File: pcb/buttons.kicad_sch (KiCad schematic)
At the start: 21 parts, among them SW1 SW_DPDT_x2, SW2 SW_DPDT_x2, SW3 RotaryEncoder, SW4 SW_DPDT_x2, SW5 SW_DPDT_x2

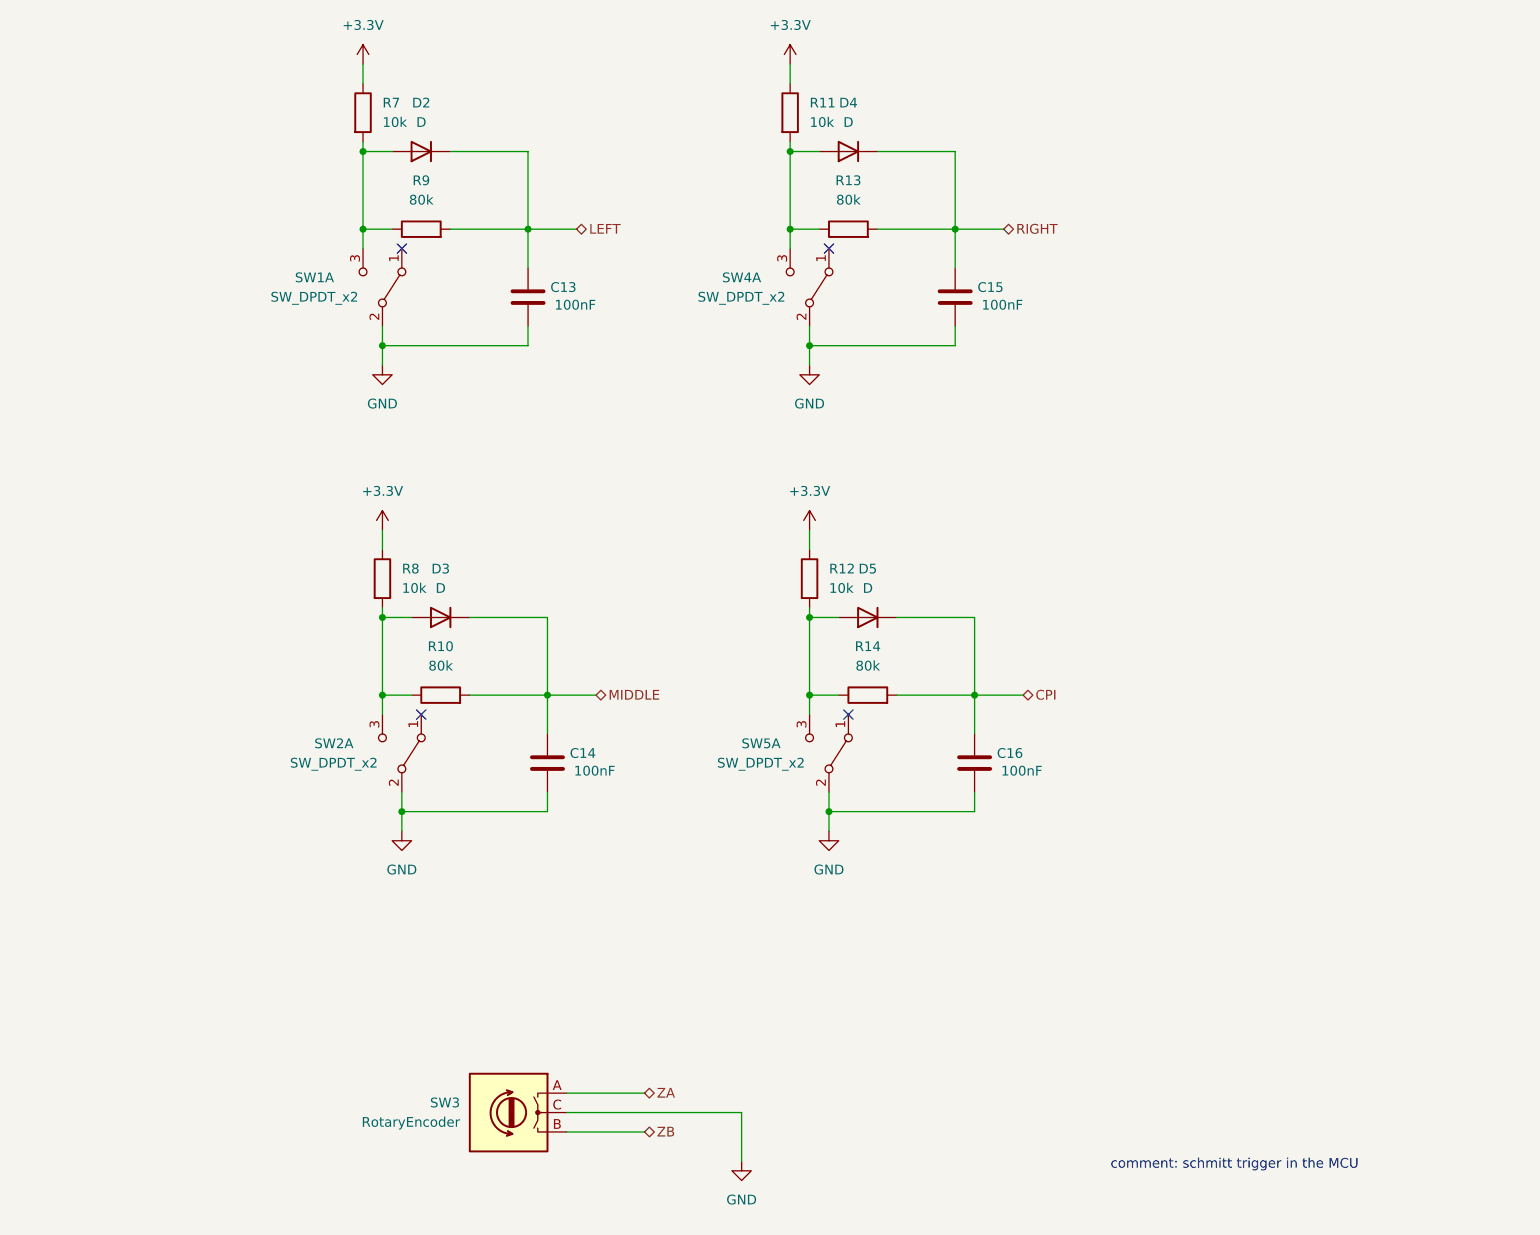
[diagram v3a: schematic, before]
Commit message: - added rotary encoder debouncing - added mouse switch and encoder footprints - changed some symbols - assigned footprints
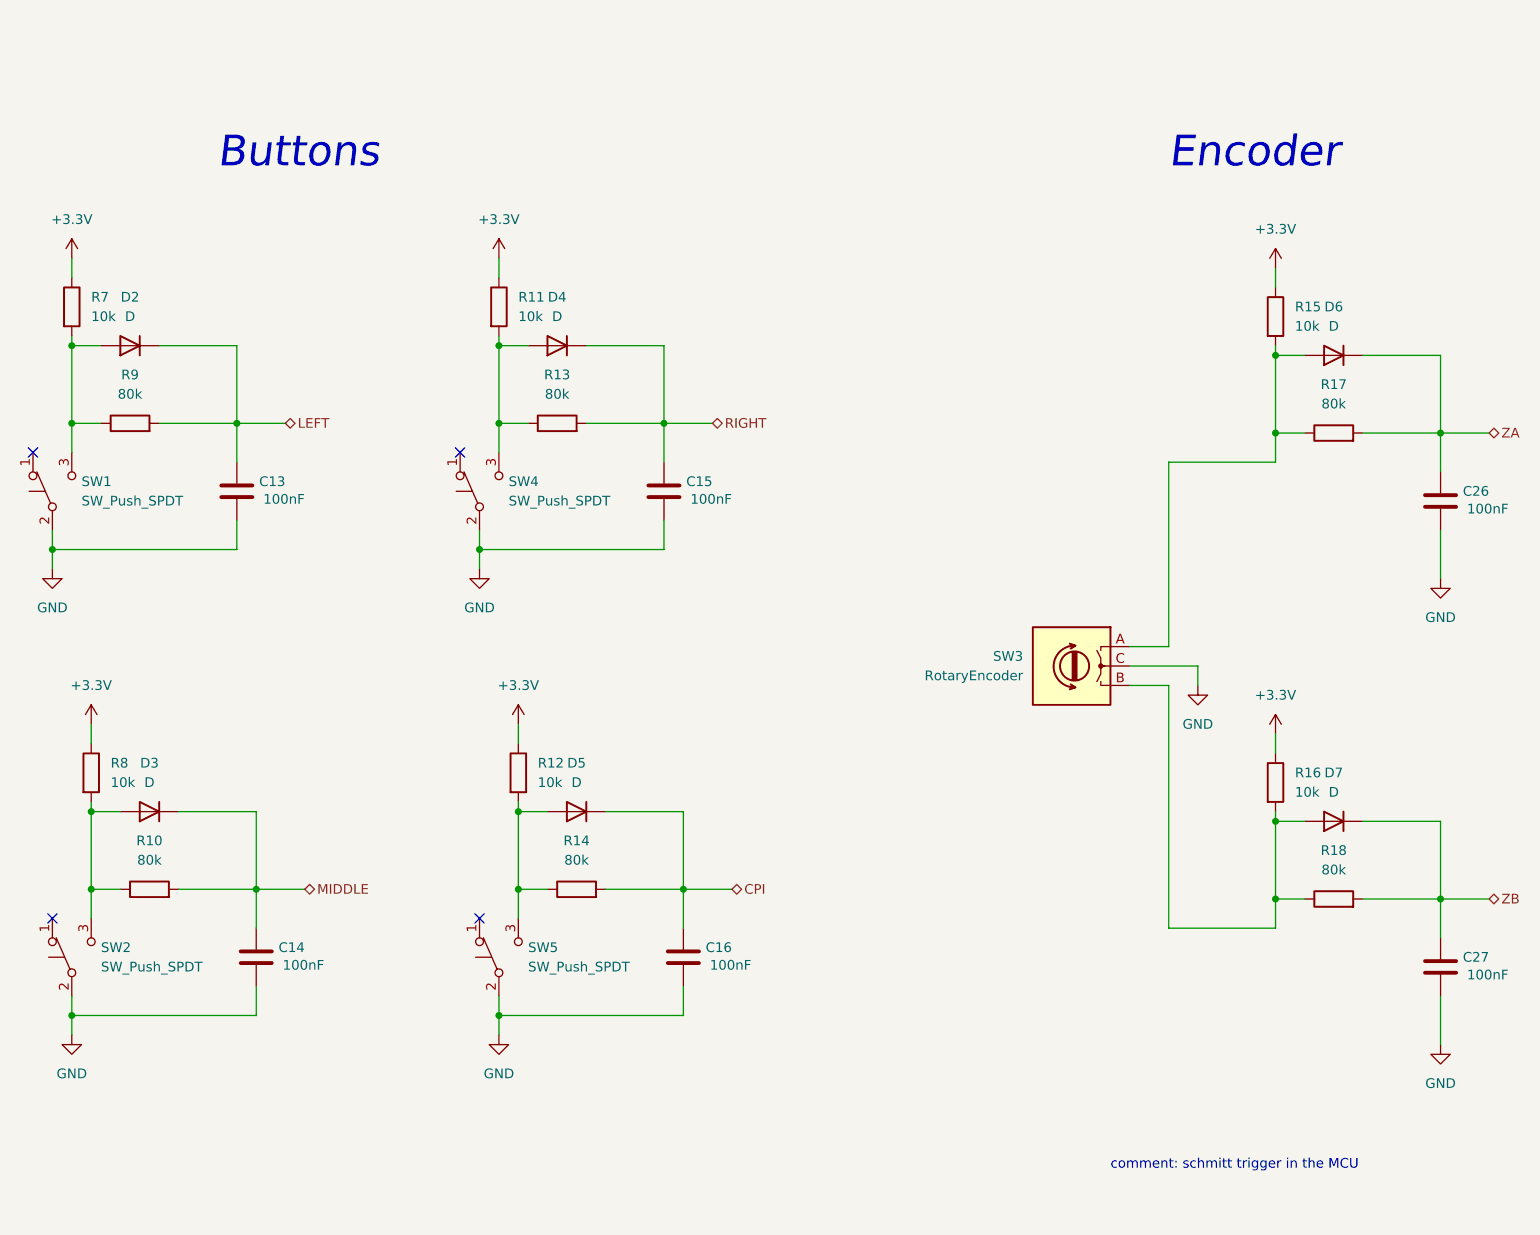
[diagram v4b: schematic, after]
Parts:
- removed SW1, SW2, SW4, SW5: SW_DPDT_x2, symbol Switch:SW_DPDT_x2
- added C26, C27: 100nF, Capacitor_SMD:C_0603_1608Metric, symbol Device:C
- added D6, D7: D, Diode_SMD:D_0603_1608Metric, symbol Device:D
- added R15, R16: 10k, Resistor_SMD:R_0603_1608Metric, symbol Device:R
- added R17, R18: 80k, Resistor_SMD:R_0603_1608Metric, symbol Device:R
- added SW1, SW2, SW4, SW5: SW_Push_SPDT, mouse:mouse_switch, symbol Switch:SW_Push_SPDT
- SW3: footprint (none) -> mouse:mouse_encoder
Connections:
- net +3V3: now also R15.1, R16.1
- net GND: now also C26.2, C27.2, SW1.2 (B), SW2.2 (B), SW4.2 (B), SW5.2 (B)
- net ZA: now also C26.1, D6.1 (K), R17.2; no longer SW3.A
- net ZB: now also C27.1, D7.1 (K), R18.2; no longer SW3.B
- net at D3.2 (A), R10.1, R8.2: now also SW2.3 (C)
- net at D2.2 (A), R7.2, R9.1: now also SW1.3 (C)
- net at D5.2 (A), R12.2, R14.1: now also SW5.3 (C)
- net at D4.2 (A), R11.2, R13.1: now also SW4.3 (C)
- new net: D7.2 (A), R16.2, R18.1, SW3.B
- new net: D6.2 (A), R15.2, R17.1, SW3.A
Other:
- note added: "Buttons"
- note added: "Encoder"
- moved on the sheet: C14, D3, R10, R8, SW3

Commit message: added LCSC part numbers and assigned footprints
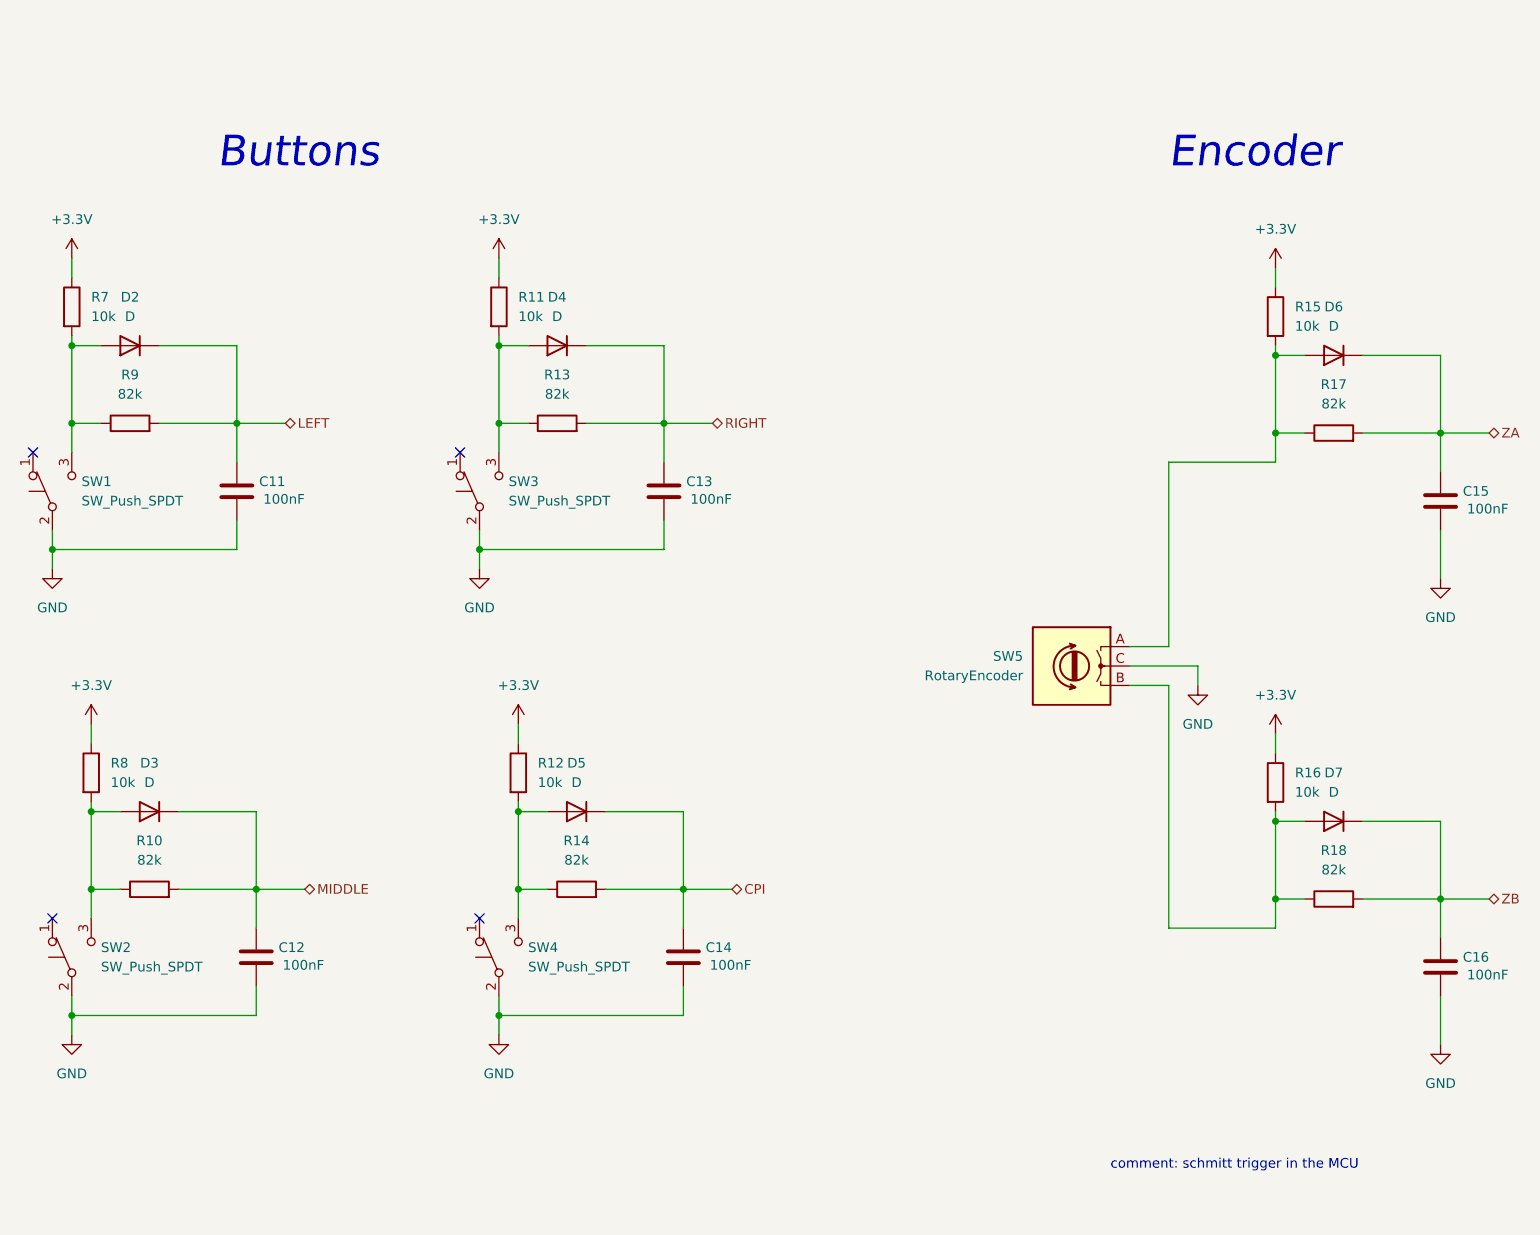
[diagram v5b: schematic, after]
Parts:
- C11: renamed from C13; LCSC (none) -> C14663
- C12: renamed from C14; LCSC (none) -> C14663
- C13: renamed from C15; LCSC (none) -> C14663
- C14: renamed from C16; LCSC (none) -> C14663
- C15: renamed from C26; LCSC (none) -> C14663
- C16: renamed from C27; LCSC (none) -> C14663
- D2, D3, D4, D5, D6, D7: footprint Diode_SMD:D_0603_1608Metric -> Diode_SMD:D_SOD-123F; LCSC (none) -> C64898
- R10, R13, R14, R17, R18, R9: value 80k -> 82k; LCSC (none) -> C23254
- R11, R12, R15, R16, R7, R8: LCSC (none) -> C25804
- renumbered SW4 to SW3, SW5 to SW4, SW3 to SW5

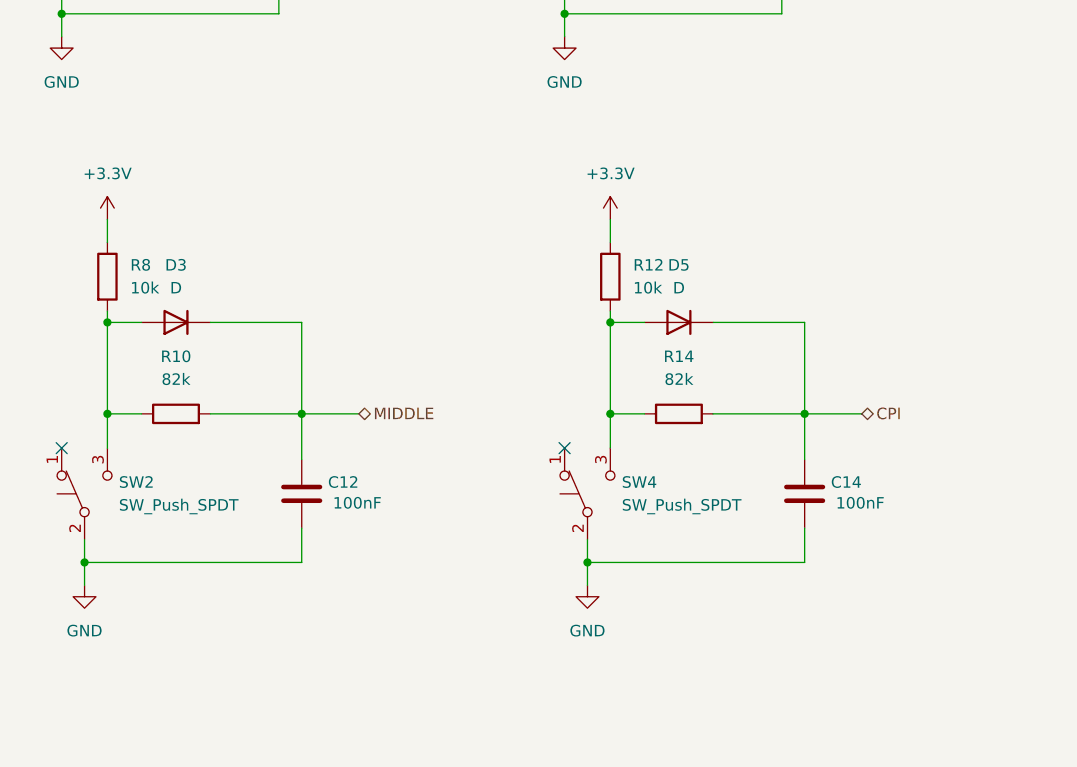
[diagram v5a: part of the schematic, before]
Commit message: - cleaned up schematics - roughly arranged components on pcb - added pcb outline
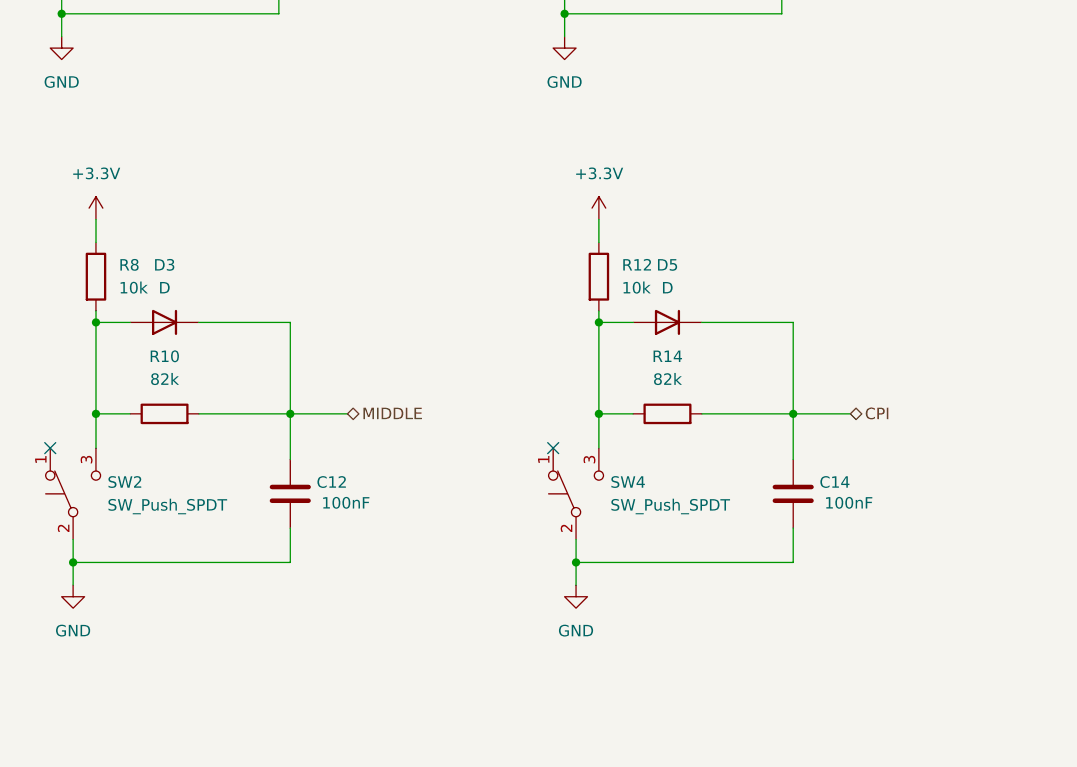
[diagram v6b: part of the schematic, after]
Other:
- moved on the sheet: C12, C14, D3, D5, R10, R12, R14, R8, SW2, SW4
